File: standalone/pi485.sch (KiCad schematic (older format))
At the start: 27 parts, among them J1 RS485, P1 Rasperry Pi, P2 PWR, P3 TERM, P4 RO, Q1 2N4401, Q2 2N4401, Q3 2N4401, U1 NE555, U2 MAX485

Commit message: Low-side NPN switching. We'll see if things 'floating' causes issues... if so, I'll have to order a few PNP's to use for high-side switching.
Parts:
- Q1, Q2, Q3: symbol BC413 -> Q_NPN_EBC
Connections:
- net GND: now also Q3.1 (E); no longer C1.2, C2.2, C3.2, D1.1 (K), D2.1 (K), D3.1 (K), P4.1 (P1), Q1.3 (E), Q2.3 (E), U1.1 (GND), U2.5 (VSS)
- net VCC: now also C1.2, C2.2, R1.2, R2.2, R3.2, R7.2, U1.4 (R), U1.8 (VCC), U2.8 (VDD); no longer Q3.1 (C)
- net at D2.2 (A), R3.1: now also Q1.3 (C); no longer Q1.1 (C)
- net at D3.2 (A), R7.1: now also Q2.3 (C); no longer Q2.1 (C)
- new net: C1.1, C2.1, C3.2, D1.1 (K), D2.1 (K), D3.1 (K), P4.1 (P1), Q1.1 (E), Q2.1 (E), Q3.3 (C), U1.1 (GND), U2.5 (VSS)
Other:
- moved on the sheet: C1, C2, D1, R1, R10
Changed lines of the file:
@@
 L PWR_FLAG #FLG02
 U 1 1 586E8329
-P 2150 2150
-F 0 "#FLG02" H 2150 2245 50  0001 C CNN
-F 1 "PWR_FLAG" H 2150 2330 50  0000 C CNN
-F 2 "" H 2150 2150 50  0000 C CNN
-F 3 "" H 2150 2150 50  0000 C CNN
-	1    2150 2150
+P 2150 1700
+F 0 "#FLG02" H 2150 1795 50  0001 C CNN
+F 1 "PWR_FLAG" H 2150 1880 50  0000 C CNN
+F 2 "" H 2150 1700 50  0000 C CNN
+F 3 "" H 2150 1700 50  0000 C CNN
+	1    2150 1700
 	0    -1   -1   0
 $EndComp
@@
 L VCC #PWR04
 U 1 1 586E83C6
-P 2150 1850
-F 0 "#PWR04" H 2150 1700 50  0001 C CNN
-F 1 "VCC" H 2150 2000 50  0000 C CNN
-F 2 "" H 2150 1850 50  0000 C CNN
-F 3 "" H 2150 1850 50  0000 C CNN
-	1    2150 1850
+P 2150 1500
+F 0 "#PWR04" H 2150 1350 50  0001 C CNN
+F 1 "VCC" H 2150 1650 50  0000 C CNN
+F 2 "" H 2150 1500 50  0000 C CNN
+F 3 "" H 2150 1500 50  0000 C CNN
+	1    2150 1500
 	1    0    0    -1
 $EndComp
@@
 L GND #PWR05
 U 1 1 586E84AD
-P 2900 5550
-F 0 "#PWR05" H 2900 5300 50  0001 C CNN
-F 1 "GND" H 2900 5400 50  0000 C CNN
-F 2 "" H 2900 5550 50  0000 C CNN
-F 3 "" H 2900 5550 50  0000 C CNN
-	1    2900 5550
+P 5500 6150
+F 0 "#PWR05" H 5500 5900 50  0001 C CNN
+F 1 "GND" H 5500 6000 50  0000 C CNN
+F 2 "" H 5500 6150 50  0000 C CNN
+F 3 "" H 5500 6150 50  0000 C CNN
+	1    5500 6150
 	1    0    0    -1
 $EndComp
@@
 L R R1
 U 1 1 586E84C4
-P 6200 1550
-F 0 "R1" H 6280 1550 50  0000 C CNN
-F 1 "200" V 6200 1550 50  0000 C CNN
-F 2 "Resistors_THT:Resistor_Horizontal_RM10mm" V 6350 850 50  0001 C CNN
-F 3 "" H 6200 1550 50  0000 C CNN
-	1    6200 1550
-	1    0    0    -1
+P 7400 3800
+F 0 "R1" H 7480 3800 50  0000 C CNN
+F 1 "200" V 7400 3800 50  0000 C CNN
+F 2 "Resistors_THT:Resistor_Horizontal_RM10mm" V 7550 3100 50  0001 C CNN
+F 3 "" H 7400 3800 50  0000 C CNN
+	1    7400 3800
+	-1   0    0    1
 $EndComp
 $Comp
 L LED D1
 U 1 1 586E8531
-P 6200 1250
-F 0 "D1" H 6200 1350 50  0000 C CNN
-F 1 "PWR" V 6200 1100 50  0000 C CNN
-F 2 "LEDs:LED-3MM" H 6150 1050 50  0001 C CNN
-F 3 "" H 6200 1250 50  0000 C CNN
-	1    6200 1250
-	0    1    1    0
+P 7400 4100
+F 0 "D1" H 7400 4200 50  0000 C CNN
+F 1 "PWR" V 7400 3950 50  0000 C CNN
+F 2 "LEDs:LED-3MM" H 7350 3900 50  0001 C CNN
+F 3 "" H 7400 4100 50  0000 C CNN
+	1    7400 4100
+	0    -1   -1   0
 $EndComp
 $Comp
@@
 $EndComp
 $Comp
-L GND #PWR06
-U 1 1 586E98F0
-P 5500 5650
-F 0 "#PWR06" H 5500 5400 50  0001 C CNN
-F 1 "GND" H 5500 5500 50  0000 C CNN
-F 2 "" H 5500 5650 50  0000 C CNN
-F 3 "" H 5500 5650 50  0000 C CNN
-	1    5500 5650
-	1    0    0    -1
-$EndComp
-$Comp
 L MAX485 U2
 U 1 1 586EA024
@@
 $EndComp
 $Comp
-L GND #PWR07
-U 1 1 586EB44F
-P 7100 3500
-F 0 "#PWR07" H 7100 3250 50  0001 C CNN
-F 1 "GND" H 7100 3350 50  0000 C CNN
-F 2 "" H 7100 3500 50  0000 C CNN
-F 3 "" H 7100 3500 50  0000 C CNN
-	1    7100 3500
-	1    0    0    -1
-$EndComp
-$Comp
-L VCC #PWR08
-U 1 1 586EB484
-P 5000 2000
-F 0 "#PWR08" H 5000 1850 50  0001 C CNN
-F 1 "VCC" H 5000 2150 50  0000 C CNN
-F 2 "" H 5000 2000 50  0000 C CNN
-F 3 "" H 5000 2000 50  0000 C CNN
-	1    5000 2000
-	1    0    0    -1
-$EndComp
-$Comp
 L R R5
 U 1 1 586EB6FC
@@
 GND
 $Comp
-L GND #PWR09
-U 1 1 586F0172
-P 8250 1900
-F 0 "#PWR09" H 8250 1650 50  0001 C CNN
-F 1 "GND" H 8250 1750 50  0000 C CNN
-F 2 "" H 8250 1900 50  0000 C CNN
-F 3 "" H 8250 1900 50  0000 C CNN
-	1    8250 1900
-	1    0    0    -1
-$EndComp
-$Comp
-L VCC #PWR010
+L VCC #PWR06
 U 1 1 586F01EA
 P 8250 3300
-F 0 "#PWR010" H 8250 3150 50  0001 C CNN
+F 0 "#PWR06" H 8250 3150 50  0001 C CNN
 F 1 "VCC" H 8250 3450 50  0000 C CNN
 F 2 "" H 8250 3300 50  0000 C CNN
@@
 $EndComp
 $Comp
-L BC413 Q1
+L Q_NPN_EBC Q1
 U 1 1 5876C3F8
 P 3100 4200
@@
 $EndComp
 $Comp
-L BC413 Q2
+L Q_NPN_EBC Q2
 U 1 1 5876C45D
 P 4000 4400
@@
 L C C2
 U 1 1 5876F3DF
-P 7050 1400
-F 0 "C2" V 7150 1550 50  0000 C CNN
-F 1 "0.1uF" V 7150 1250 50  0000 C CNN
-F 2 "Capacitors_THT:C_Rect_L7_W2.5_P5" V 7250 1100 50  0001 C CNN
-F 3 "" H 7050 1400 50  0000 C CNN
-	1    7050 1400
+P 8250 3950
+F 0 "C2" V 8350 4100 50  0000 C CNN
+F 1 "0.1uF" V 8350 3800 50  0000 C CNN
+F 2 "Capacitors_THT:C_Rect_L7_W2.5_P5" V 8450 3650 50  0001 C CNN
+F 3 "" H 8250 3950 50  0000 C CNN
+	1    8250 3950
 	-1   0    0    1
 $EndComp
@@
 L C C1
 U 1 1 5876F5F2
-P 6600 1400
-F 0 "C1" V 6700 1550 50  0000 C CNN
-F 1 "10uF" V 6700 1250 50  0000 C CNN
-F 2 "Capacitors_THT:C_Radial_D5_L11_P2" V 6800 1100 50  0001 C CNN
-F 3 "" H 6600 1400 50  0000 C CNN
-	1    6600 1400
+P 7800 3950
+F 0 "C1" V 7900 4100 50  0000 C CNN
+F 1 "10uF" V 7900 3800 50  0000 C CNN
+F 2 "Capacitors_THT:C_Radial_D5_L11_P2" V 8000 3650 50  0001 C CNN
+F 3 "" H 7800 3950 50  0000 C CNN
+	1    7800 3950
 	-1   0    0    1
 $EndComp
@@
 L R R10
 U 1 1 587FCED5
-P 5600 2600
-F 0 "R10" V 5500 2600 50  0000 C CNN
-F 1 "270" V 5600 2600 50  0000 C CNN
-F 2 "Resistors_THT:Resistor_Horizontal_RM10mm" V 5750 1900 50  0001 C CNN
-F 3 "" H 5600 2600 50  0000 C CNN
-	1    5600 2600
-	1    0    0    -1
-$EndComp
-$Comp
-L BC413 Q3
+P 5050 5950
+F 0 "R10" V 4950 5950 50  0000 C CNN
+F 1 "270" V 5050 5950 50  0000 C CNN
+F 2 "Resistors_THT:Resistor_Horizontal_RM10mm" V 5200 5250 50  0001 C CNN
+F 3 "" H 5050 5950 50  0000 C CNN
+	1    5050 5950
+	0    1    1    0
+$EndComp
+$Comp
+L Q_NPN_EBC Q3
 U 1 1 587FCF77
-P 5600 2100
-F 0 "Q3" V 5836 2100 50  0000 C CNN
-F 1 "2N4401" V 5500 1850 50  0000 C CNN
-F 2 "TO_SOT_Packages_THT:TO-92_Inline_Wide" V 6018 2100 50  0001 C CIN
-F 3 "" H 5600 2100 50  0000 L CNN
-	1    5600 2100
-	0    -1   -1   0
-$EndComp
-Connection ~ 2150 2150
+P 5400 5950
+F 0 "Q3" V 5636 5950 50  0000 C CNN
+F 1 "2N4401" V 5300 5700 50  0000 C CNN
+F 2 "TO_SOT_Packages_THT:TO-92_Inline_Wide" V 5818 5950 50  0001 C CIN
+F 3 "" H 5400 5950 50  0000 L CNN
+	1    5400 5950
+	1    0    0    -1
+$EndComp
+Text Label 2900 2150 3    60   ~ 0
+(485PWR)_GPIO18
+$Comp
+L GND #PWR07
+U 1 1 586F0172
+P 8250 1900
+F 0 "#PWR07" H 8250 1650 50  0001 C CNN
+F 1 "GND" H 8250 1750 50  0000 C CNN
+F 2 "" H 8250 1900 50  0000 C CNN
+F 3 "" H 8250 1900 50  0000 C CNN
+	1    8250 1900
+	1    0    0    -1
+$EndComp
+Connection ~ 2150 1700
 Wire Wire Line
 	2600 2150 2600 3200
@@
 Wire Wire Line
 	5000 5450 6000 5450
-Wire Wire Line
-	5500 5250 5500 5650
 Connection ~ 5500 5450
 Wire Wire Line
@@
 	2500 2150 2500 3200
 Wire Wire Line
-	2150 1850 2150 2800
+	2150 1500 2150 2800
 Wire Wire Line
 	2150 2900 2150 3250
@@
 	8000 2600 8000 2700
 Wire Wire Line
-	7100 3200 7100 3500
+	7100 3200 7100 5750
 Wire Wire Line
 	7500 2650 7500 2300
@@
 	2900 4300 2900 4850
 Wire Wire Line
-	2900 5150 2900 5550
+	2900 5150 2900 5750
 Wire Wire Line
 	2800 4300 2900 4300
@@
 Wire Wire Line
 	5000 5350 5000 4850
-Text Label 2900 2150 3    60   ~ 0
-(485PWR)_GPIO18
-Wire Wire Line
-	2900 2150 2900 2900
-Wire Wire Line
-	2900 2900 5600 2900
-Wire Wire Line
-	5600 2900 5600 2750
-Wire Wire Line
-	5800 2000 7100 2000
-Wire Wire Line
-	7100 2000 7100 2300
-Wire Wire Line
-	6200 3550 6200 1700
-Wire Wire Line
-	8250 1000 8250 1900
-Connection ~ 6200 2000
-Wire Wire Line
-	2500 3550 6200 3550
-Wire Wire Line
-	6200 1000 8250 1000
-Wire Wire Line
-	6200 1000 6200 1100
+Connection ~ 7400 4550
+Wire Wire Line
+	2300 3550 8250 3550
+Wire Wire Line
+	7400 3550 7400 3650
 Wire Wire Line
 	2900 5400 4200 5400
 Wire Wire Line
-	6600 2000 6600 1550
-Wire Wire Line
-	7050 1550 7050 2000
-Connection ~ 7050 2000
-Wire Wire Line
-	7050 1250 7050 1000
-Connection ~ 7050 1000
-Wire Wire Line
-	6600 1250 6600 1000
-Connection ~ 6600 1000
-Connection ~ 6600 2000
-Wire Wire Line
-	5000 2000 5400 2000
-Wire Wire Line
-	5600 2300 5600 2450
+	7800 5750 7800 4100
+Wire Wire Line
+	8250 4550 8250 4100
+Connection ~ 8250 4550
+Wire Wire Line
+	8250 3550 8250 3800
+Connection ~ 8250 3550
+Wire Wire Line
+	7800 3800 7800 3550
+Connection ~ 7800 3550
+Connection ~ 7800 4550
 Connection ~ 5500 3550
 Wire Wire Line
 	6400 5450 6300 5450
+Wire Wire Line
+	2900 5750 7800 5750
+Connection ~ 5500 5750
+Wire Wire Line
+	5500 5250 5500 5750
+Wire Wire Line
+	2300 3550 2300 2800
+Connection ~ 2300 2800
+Connection ~ 2500 3550
+Wire Wire Line
+	7100 2300 7100 2100
+Wire Wire Line
+	7100 2100 6200 2100
+Wire Wire Line
+	6200 2100 6200 3550
+Wire Wire Line
+	7400 4550 8250 4550
+Connection ~ 6200 3550
+Connection ~ 7400 3550
+Wire Wire Line
+	7400 4550 7400 4250
+Wire Wire Line
+	4900 5950 1800 5950
+Wire Wire Line
+	1800 5950 1800 2600
+Wire Wire Line
+	1800 2600 2900 2600
+Wire Wire Line
+	2900 2600 2900 2150
+Connection ~ 7100 5750
 $EndSCHEMATC

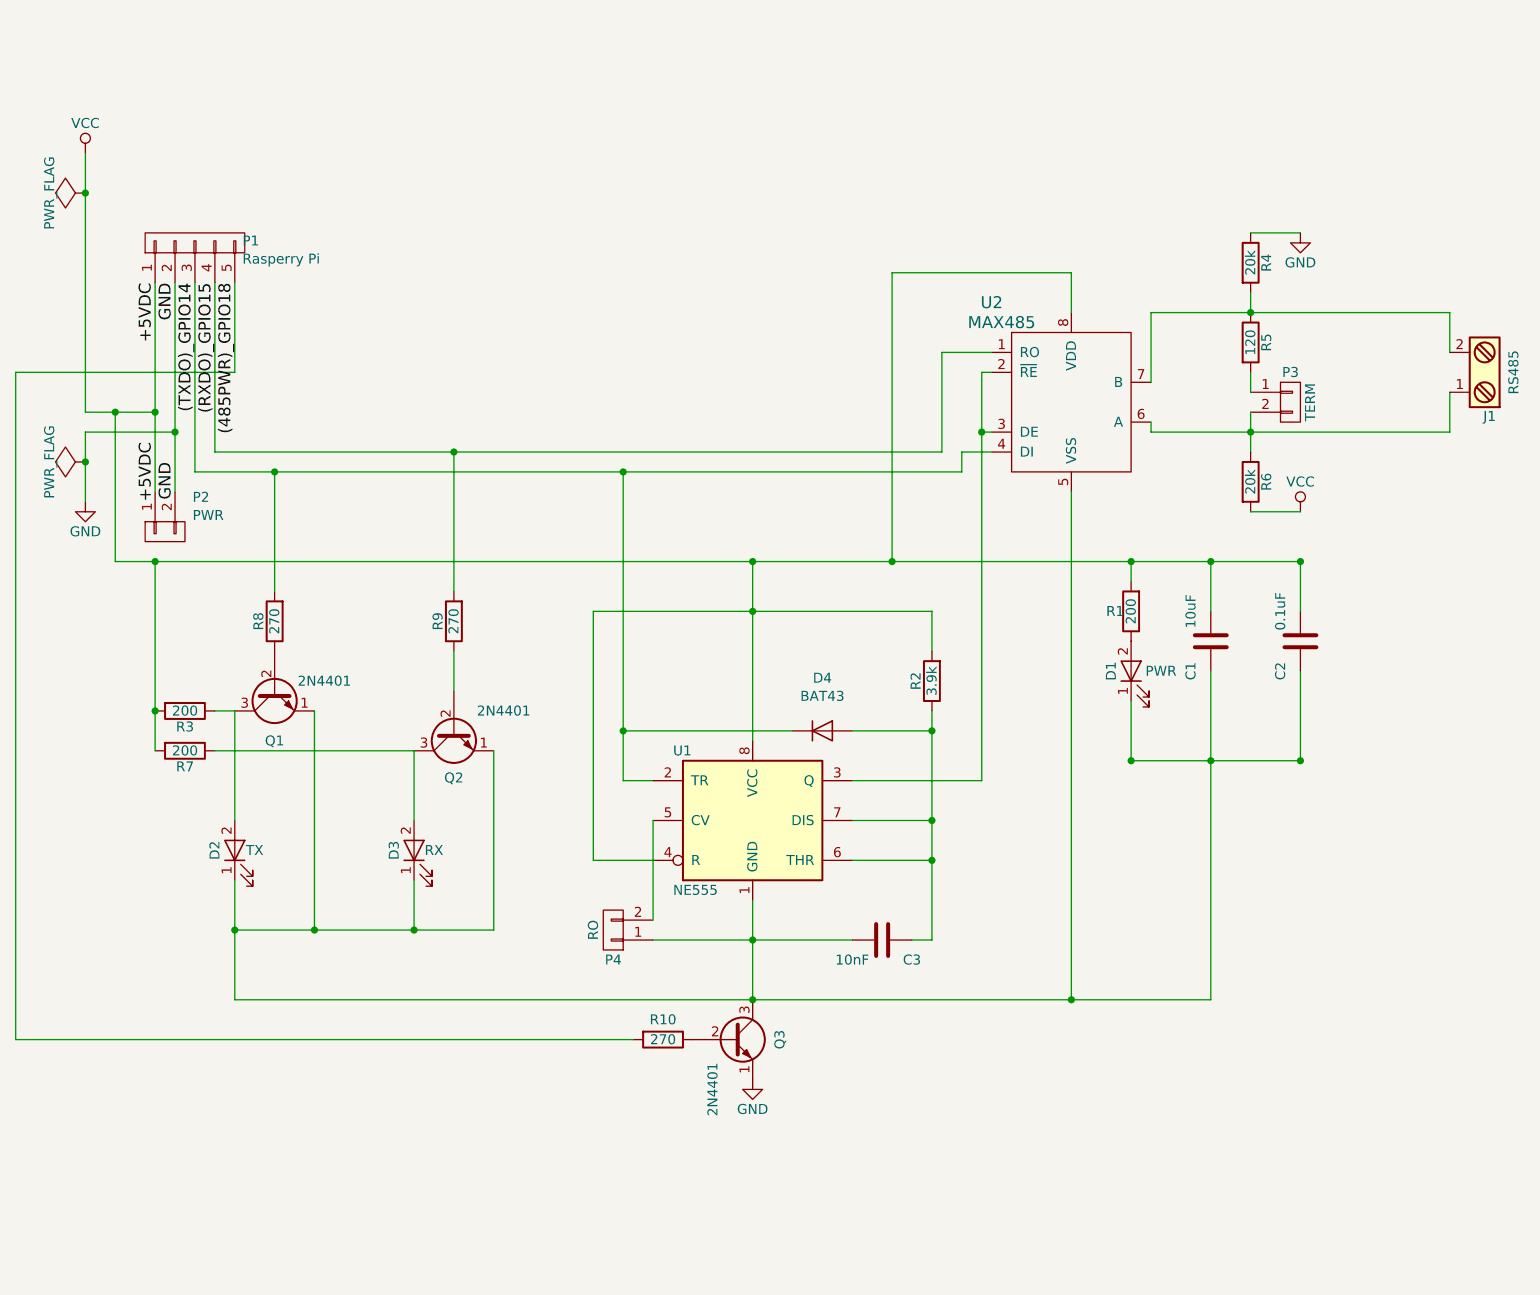
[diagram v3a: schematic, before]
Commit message: standalone reconfigured for high-side PNP switching
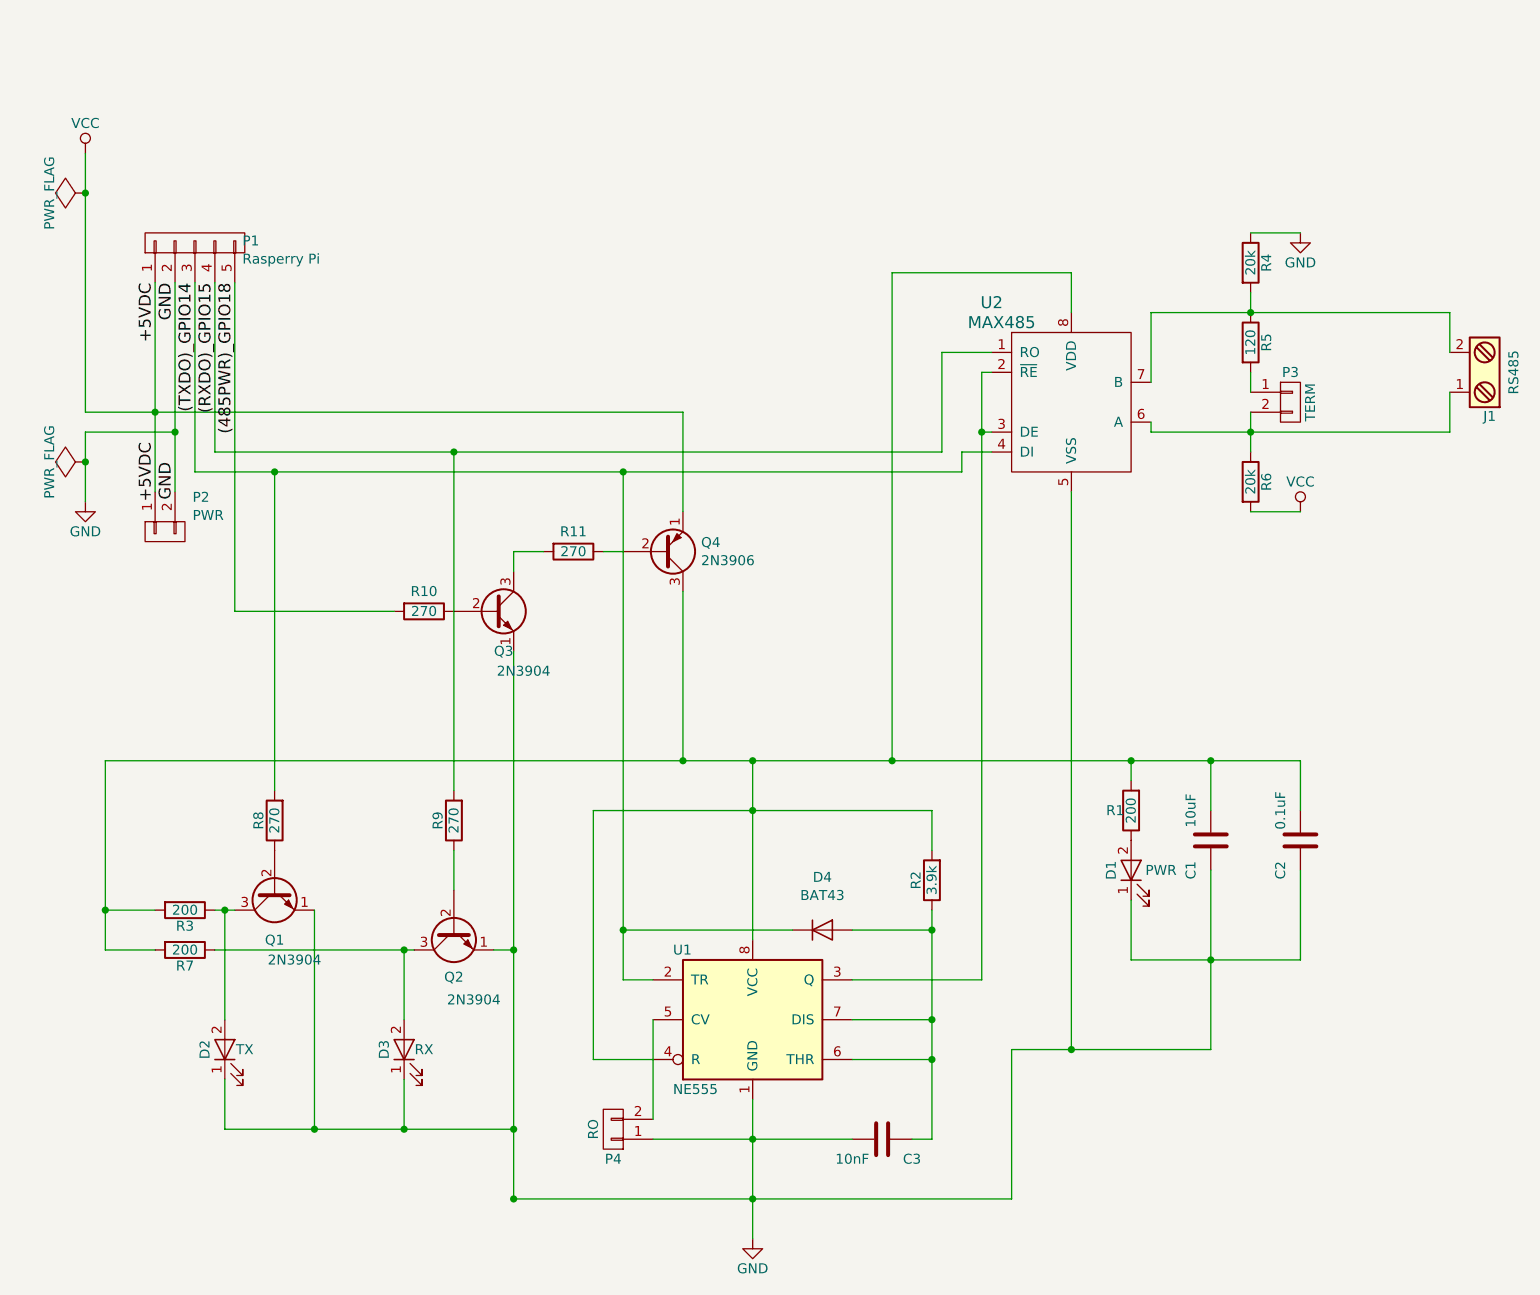
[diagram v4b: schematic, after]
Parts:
- added Q4: 2N3906, TO_SOT_Packages_THT:TO-92_Inline_Wide, symbol Q_PNP_EBC
- added R11: 270, Resistors_THT:Resistor_Horizontal_RM10mm, symbol R
- P1: footprint Socket_Strips:Socket_Strip_Angled_1x05 -> Pin_Headers:Pin_Header_Straight_1x05
- P2: footprint Socket_Strips:Socket_Strip_Angled_1x02 -> Pin_Headers:Pin_Header_Straight_1x02
- Q1, Q2, Q3: value 2N4401 -> 2N3904
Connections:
- net GND: now also C1.1, C2.1, C3.2, D1.1 (K), D2.1 (K), D3.1 (K), P4.1 (P1), Q1.1 (E), Q2.1 (E), U1.1 (GND), U2.5 (VSS)
- net VCC: now also Q4.1 (E); no longer C1.2, C2.2, R1.2, R2.2, R3.2, R7.2, U1.4 (R), U1.8 (VCC), U2.8 (VDD)
- new net: C1.2, C2.2, Q4.3 (C), R1.2, R2.2, R3.2, R7.2, U1.4 (R), U1.8 (VCC), U2.8 (VDD)
- new net: Q3.3 (C), R11.2
- new net: Q4.2 (B), R11.1
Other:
- moved on the sheet: C1, C2, C3, D1, D2, D3, D4, P4, Q1, Q2, Q3, R1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

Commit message: Esthetics and what-not...
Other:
- moved on the sheet: C1, C2, D1, R1, R2
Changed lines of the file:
@@
 L R R1
 U 1 1 586E84C4
-P 7400 4800
-F 0 "R1" H 7480 4800 50  0000 C CNN
-F 1 "200" V 7400 4800 50  0000 C CNN
-F 2 "Resistors_THT:Resistor_Horizontal_RM10mm" V 7550 4100 50  0001 C CNN
-F 3 "" H 7400 4800 50  0000 C CNN
-	1    7400 4800
+P 7400 4900
+F 0 "R1" H 7480 4900 50  0000 C CNN
+F 1 "200" V 7400 4900 50  0000 C CNN
+F 2 "Resistors_THT:Resistor_Horizontal_RM10mm" V 7550 4200 50  0001 C CNN
+F 3 "" H 7400 4900 50  0000 C CNN
+	1    7400 4900
 	-1   0    0    1
 $EndComp
@@
 L LED D1
 U 1 1 586E8531
-P 7400 5100
-F 0 "D1" H 7400 5200 50  0000 C CNN
-F 1 "PWR" V 7400 4950 50  0000 C CNN
-F 2 "LEDs:LED-3MM" H 7350 4900 50  0001 C CNN
-F 3 "" H 7400 5100 50  0000 C CNN
-	1    7400 5100
+P 7400 5200
+F 0 "D1" H 7400 5300 50  0000 C CNN
+F 1 "PWR" V 7400 5050 50  0000 C CNN
+F 2 "LEDs:LED-3MM" H 7350 5000 50  0001 C CNN
+F 3 "" H 7400 5200 50  0000 C CNN
+	1    7400 5200
 	0    -1   -1   0
 $EndComp
@@
 L R R2
 U 1 1 586E88D3
-P 6400 5150
-F 0 "R2" V 6480 5150 50  0000 C CNN
-F 1 "3.9k" V 6400 5150 50  0000 C CNN
-F 2 "Resistors_THT:Resistor_Horizontal_RM10mm" H 5500 5150 50  0001 C CNN
-F 3 "" H 6400 5150 50  0000 C CNN
-	1    6400 5150
+P 6400 5000
+F 0 "R2" V 6480 5000 50  0000 C CNN
+F 1 "3.9k" V 6400 5000 50  0000 C CNN
+F 2 "Resistors_THT:Resistor_Horizontal_RM10mm" H 5500 5000 50  0001 C CNN
+F 3 "" H 6400 5000 50  0000 C CNN
+	1    6400 5000
 	-1   0    0    1
 $EndComp
@@
 L C C2
 U 1 1 5876F3DF
-P 8250 4950
-F 0 "C2" V 8350 5100 50  0000 C CNN
-F 1 "0.1uF" V 8350 4800 50  0000 C CNN
-F 2 "Capacitors_THT:C_Rect_L7_W2.5_P5" V 8450 4650 50  0001 C CNN
-F 3 "" H 8250 4950 50  0000 C CNN
-	1    8250 4950
+P 8250 5050
+F 0 "C2" V 8350 5200 50  0000 C CNN
+F 1 "0.1uF" V 8350 4900 50  0000 C CNN
+F 2 "Capacitors_THT:C_Rect_L7_W2.5_P5" V 8450 4750 50  0001 C CNN
+F 3 "" H 8250 5050 50  0000 C CNN
+	1    8250 5050
 	-1   0    0    1
 $EndComp
@@
 L C C1
 U 1 1 5876F5F2
-P 7800 4950
-F 0 "C1" V 7900 5100 50  0000 C CNN
-F 1 "10uF" V 7900 4800 50  0000 C CNN
-F 2 "Capacitors_THT:C_Radial_D5_L11_P2" V 8000 4650 50  0001 C CNN
-F 3 "" H 7800 4950 50  0000 C CNN
-	1    7800 4950
+P 7800 5050
+F 0 "C1" V 7900 5200 50  0000 C CNN
+F 1 "10uF" V 7900 4900 50  0000 C CNN
+F 2 "Capacitors_THT:C_Radial_D5_L11_P2" V 8000 4750 50  0001 C CNN
+F 3 "" H 7800 5050 50  0000 C CNN
+	1    7800 5050
 	-1   0    0    1
 $EndComp
@@
 	5500 4550 5500 5450
 Wire Wire Line
-	6400 5300 6400 6450
+	6400 5150 6400 6450
 Wire Wire Line
 	6400 5850 6000 5850
@@
 	5000 6050 4700 6050
 Wire Wire Line
-	4700 6050 4700 4800
-Connection ~ 5500 4800
+	4700 6050 4700 4550
 Wire Wire Line
 	2150 2800 5150 2800
@@
 Connection ~ 2600 2900
 Wire Wire Line
-	4700 4800 6400 4800
-Wire Wire Line
-	6400 4800 6400 5000
+	6400 4550 6400 4850
 Wire Wire Line
 	5700 5400 4850 5400
@@
 	5000 6350 5000 5850
 Wire Wire Line
-	7400 4550 7400 4650
-Wire Wire Line
-	7800 6000 7800 5100
-Wire Wire Line
-	8250 5550 8250 5100
-Wire Wire Line
-	8250 4550 8250 4800
-Wire Wire Line
-	7800 4550 7800 4800
+	7400 4550 7400 4750
+Wire Wire Line
+	8250 5550 8250 5200
+Wire Wire Line
+	8250 4550 8250 4900
+Wire Wire Line
+	7800 4550 7800 4900
 Connection ~ 7800 4550
 Connection ~ 7800 5550
@@
 Wire Wire Line
 	4300 6750 6800 6750
-Wire Wire Line
-	6800 6000 7800 6000
 Connection ~ 5500 6750
 Wire Wire Line
@@
 	6200 2100 6200 4550
 Wire Wire Line
-	7400 5550 8250 5550
+	7100 5550 8250 5550
 Connection ~ 6200 4550
 Connection ~ 7400 4550
 Wire Wire Line
-	7400 5550 7400 5250
+	7400 5550 7400 5350
 Wire Wire Line
 	2900 3800 2900 2150
-Connection ~ 7100 6000
 Wire Wire Line
 	2250 4550 8250 4550
@@
 Wire Wire Line
 	5150 2800 5150 3300
+Connection ~ 6400 4550
+Connection ~ 4700 4550
+Connection ~ 7100 5550
+Connection ~ 7400 5550
+Wire Wire Line
+	6800 6000 7100 6000
+Wire Wire Line
+	7800 5200 7800 5550
 $EndSCHEMATC
